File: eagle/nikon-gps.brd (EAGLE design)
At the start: 29.5 x 29.5 mm, 8 parts, among them IC1 GPS-A2235-H, IC2 LP2985SOT, IC3 MAX3370

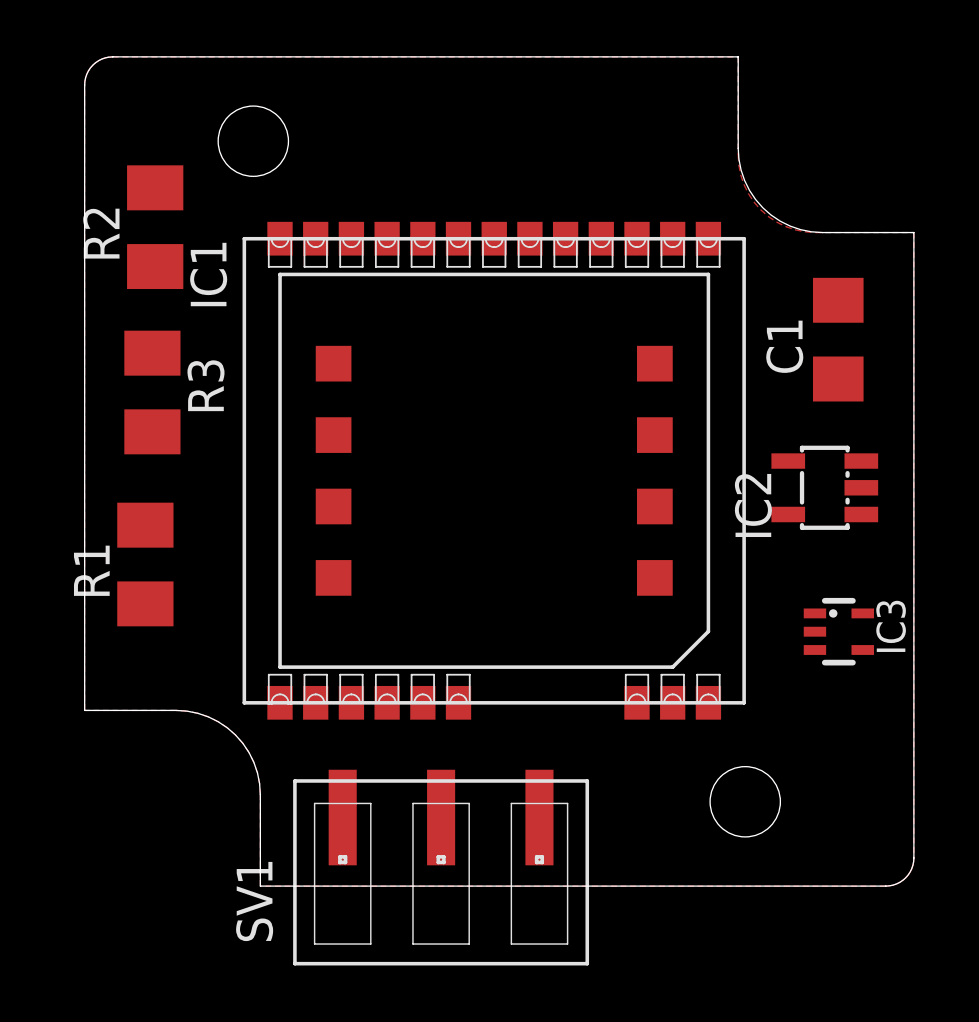
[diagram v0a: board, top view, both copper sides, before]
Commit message: First stab at a PCB layout.
The part placement might still be optimized, esp. if we consider adding
a Status-LED.
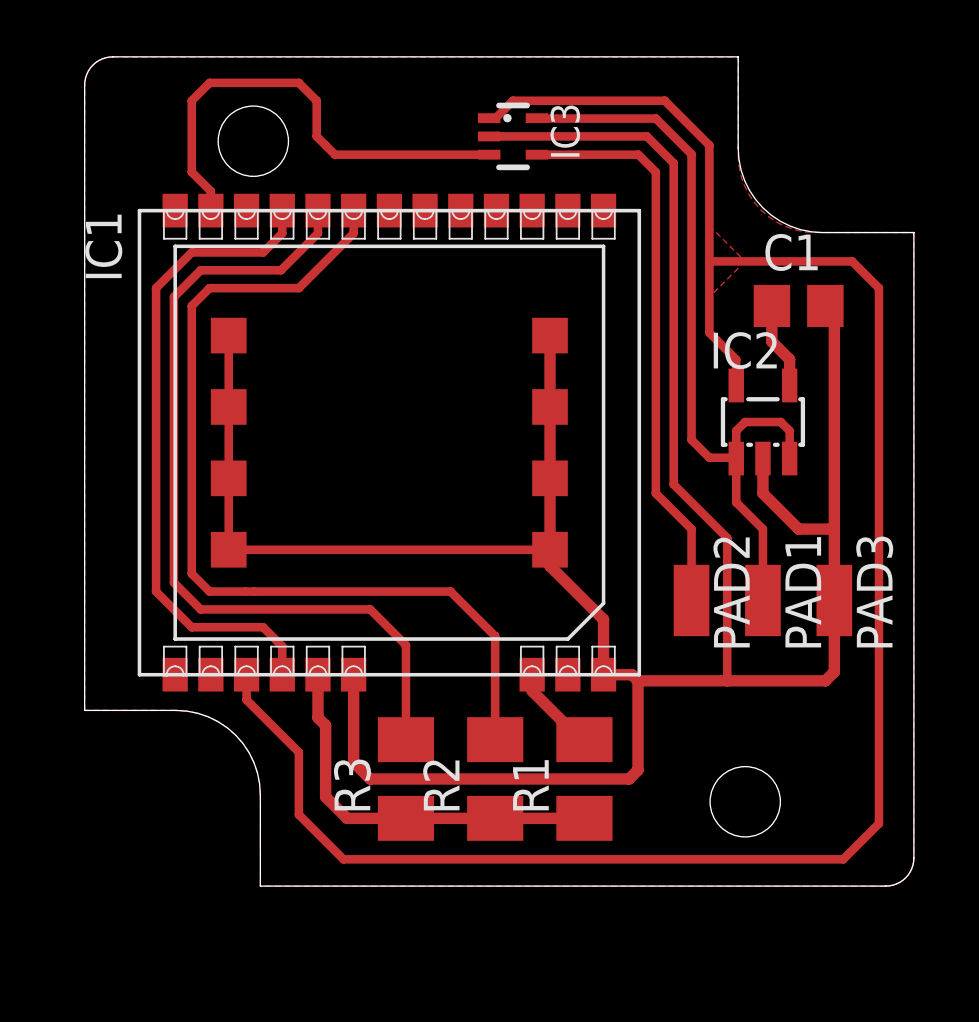
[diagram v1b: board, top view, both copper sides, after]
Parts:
- removed SV1: AKL059-03, selfmade:AKL059-03
- added PAD1, PAD2, PAD3: (no value), wirepad:SMD1,27-2,54
- C1: device rcl:C1206 -> rcl:C0805
- moved R2 23.1 mm to (14.6, 3.81)
- moved IC3 21.1 mm to (15.2, 26.7)
- moved R1 17.4 mm to (17.8, 3.81)
- moved R3 16.4 mm to (11.4, 3.81), turned to 90 degrees
- moved IC1 3.86 mm to (4.49, 11.3)
- moved IC2 3.21 mm to (24.1, 16.5), turned to 0 degrees
- moved C1 1.85 mm to (25.4, 20.6), turned to 0 degrees
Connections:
- net +5V: now also PAD1.1; no longer SV1.1
- net GND: now also PAD3.1; no longer SV1.3
- net N$3: now also PAD2.1; no longer SV1.2
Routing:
- net GND: track 0.00 -> 101.0 mm
- net +3V3: track 0.00 -> 70.7 mm
- net N$6: track 0.00 -> 32.6 mm
- net N$5: track 0.00 -> 29.6 mm
- net +5V: track 0.00 -> 27.6 mm
- net N$7: track 0.00 -> 23.2 mm
- net N$3: track 0.00 -> 20.3 mm
- net N$2: track 0.00 -> 16.8 mm
- net VOUT: track 0.00 -> 14.0 mm
- net N$4: track 0.00 -> 3.16 mm
- net N$1: track 0.00 -> 3.09 mm
- added copper zone on layer 1, net +3V3
- added copper zone on layer 1, net GND
- removed copper zone on layer 1, net GND_NOT_YET

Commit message: Adding missing capacitors for LP2985 voltage regulator.
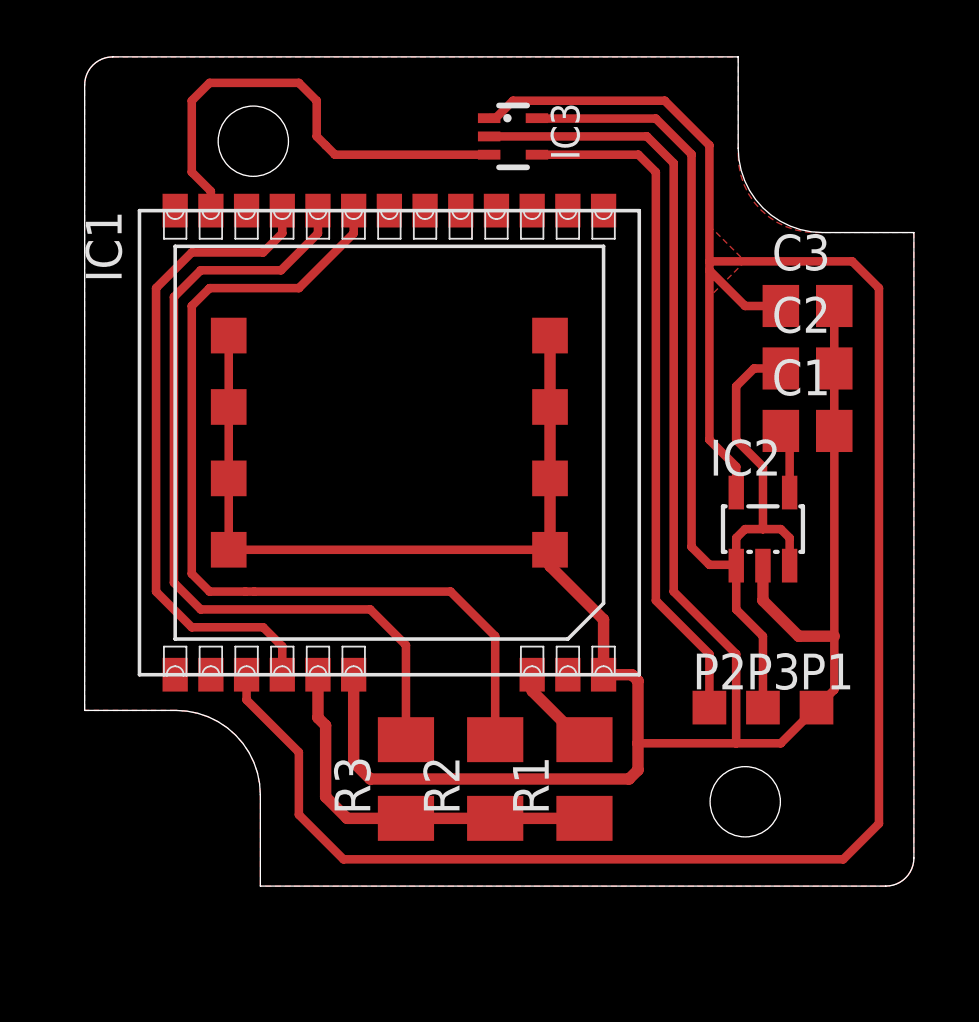
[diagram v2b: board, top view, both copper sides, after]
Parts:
- removed PAD1, PAD2, PAD3: (no value), wirepad:SMD1,27-2,54
- added C2: 1u, rcl:C0805
- added C3: 2u2, rcl:C0805
- added P1, P2, P3: TPTP12SQ, testpad:TP12SQ
- C1: value 100n -> 10n
- moved C1 4.46 mm to (25.7, 16.2)
- moved IC2 3.81 mm to (24.1, 12.7)
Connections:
- net +3V3: now also C3.1
- net +5V: now also C2.1, P3.TP; no longer PAD1.1
- net GND: now also C2.2, C3.2, P1.TP; no longer PAD3.1
- net N$3: now also P2.TP; no longer PAD2.1
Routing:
- net +5V: track 27.6 -> 38.8 mm
- net +3V3: track 70.7 -> 77.6 mm
- net N$3: track 20.3 -> 24.3 mm
- net GND: track 101.0 -> 104.5 mm
- net N$1: track 3.09 -> 2.32 mm

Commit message: Slightly adjusting placement of cable soldering pads.
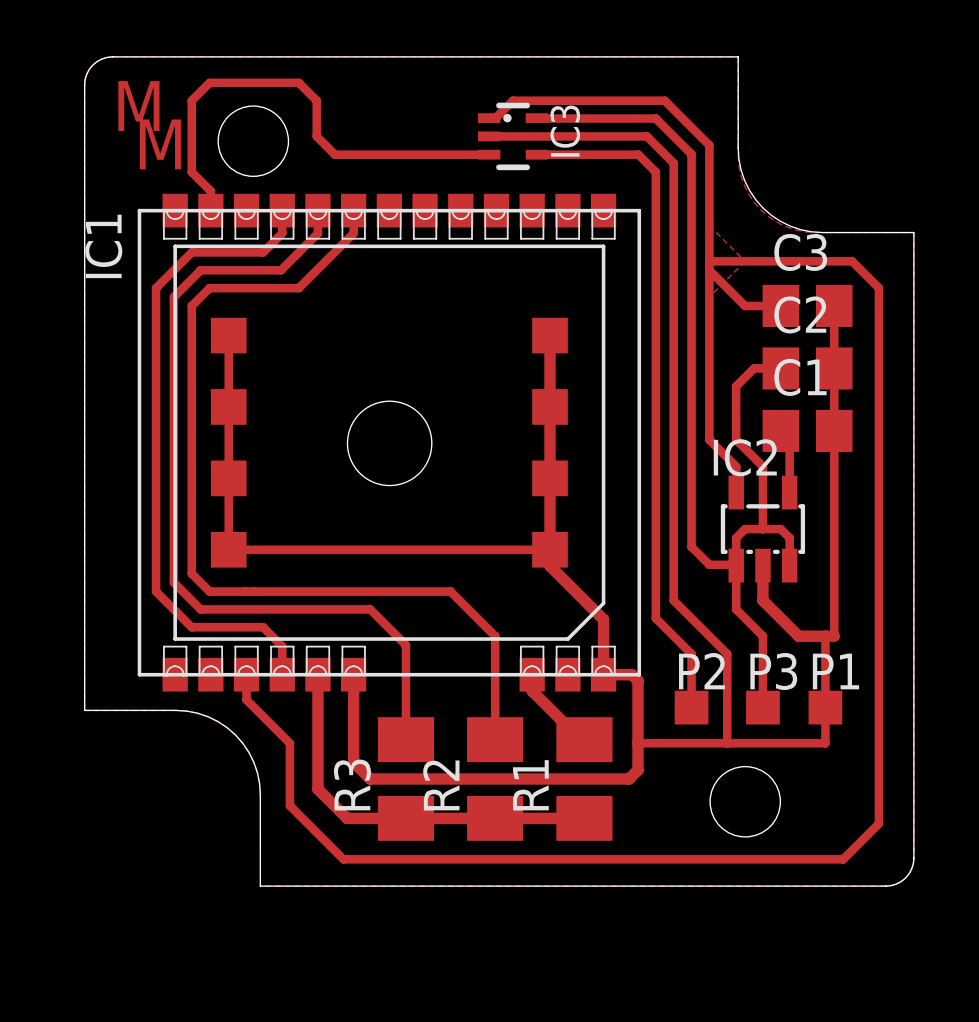
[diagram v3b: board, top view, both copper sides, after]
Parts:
- moved P2 0.64 mm to (21.6, 6.35)
- moved P1 0.32 mm to (26.4, 6.35)
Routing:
- net GND: track 104.5 -> 105.1 mm
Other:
- board text added: "M"
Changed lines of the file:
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@@
 <hole x="23.5" y="3" drill="2.5"/>
 <hole x="6" y="26.5" drill="2.5"/>
+<hole x="10.85" y="15.75" drill="3"/>
+<text x="0.98425" y="26.8605" size="1.778" layer="1" font="vector" ratio="10">M</text>
+<text x="1.74625" y="25.49525" size="1.778" layer="1" font="vector" ratio="10">M</text>
 </plain>
 <attributes>
@@
 <attribute name="TP_SIGNAL_NAME" value="" x="24.13" y="6.35" size="1.778" layer="27" display="off"/>
 </element>
-<element name="P2" library="testpad" package="TP12SQ" value="TPTP12SQ" x="22.225" y="6.35">
-<attribute name="TP_SIGNAL_NAME" value="" x="22.225" y="6.35" size="1.778" layer="27" display="off"/>
+<element name="P2" library="testpad" package="TP12SQ" value="TPTP12SQ" x="21.59" y="6.35">
+<attribute name="TP_SIGNAL_NAME" value="" x="21.59" y="6.35" size="1.778" layer="27" display="off"/>
 </element>
-<element name="P1" library="testpad" package="TP12SQ" value="TPTP12SQ" x="26.035" y="6.35">
-<attribute name="TP_SIGNAL_NAME" value="" x="26.035" y="6.35" size="1.778" layer="27" display="off"/>
+<element name="P1" library="testpad" package="TP12SQ" value="TPTP12SQ" x="26.3525" y="6.35">
+<attribute name="TP_SIGNAL_NAME" value="" x="26.3525" y="6.35" size="1.778" layer="27" display="off"/>
 </element>
 </elements>
@@
 <wire x1="10.16" y1="3.81" x2="19.3675" y2="3.81" width="0.4064" layer="1"/>
 <wire x1="19.3675" y1="3.81" x2="19.685" y2="4.1275" width="0.4064" layer="1"/>
-<wire x1="18.46" y1="7.52" x2="19.4675" y2="7.52" width="0.4064" layer="1"/>
 <wire x1="19.4675" y1="7.52" x2="19.685" y2="7.3025" width="0.4064" layer="1"/>
 <wire x1="19.685" y1="7.3025" x2="19.685" y2="5.08" width="0.4064" layer="1"/>
@@
 <wire x1="14.39" y1="26.67" x2="20.0025" y2="26.67" width="0.3048" layer="1"/>
 <wire x1="20.0025" y1="26.67" x2="20.955" y2="25.7175" width="0.3048" layer="1"/>
-<wire x1="20.955" y1="25.7175" x2="20.955" y2="10.4775" width="0.3048" layer="1"/>
-<wire x1="20.955" y1="10.4775" x2="23.1775" y2="8.255" width="0.3048" layer="1"/>
+<wire x1="20.955" y1="25.7175" x2="20.955" y2="10.16" width="0.3048" layer="1"/>
+<wire x1="20.955" y1="10.16" x2="22.86" y2="8.255" width="0.3048" layer="1"/>
 <wire x1="5.125" y1="19.585" x2="5.125" y2="17.045" width="0.3048" layer="1"/>
 <wire x1="5.125" y1="17.045" x2="5.125" y2="14.505" width="0.3048" layer="1"/>
@@
 <wire x1="24.13" y1="11.4" x2="24.13" y2="10.16" width="0.4064" layer="1"/>
 <wire x1="24.13" y1="10.16" x2="25.4" y2="8.89" width="0.4064" layer="1"/>
-<wire x1="25.4" y1="8.89" x2="26.67" y2="8.89" width="0.4064" layer="1"/>
+<wire x1="25.4" y1="8.89" x2="26.3525" y2="8.89" width="0.4064" layer="1"/>
 <polygon width="0.3048" layer="1" spacing="0.6096" isolate="0.4064">
 <vertex x="0" y="6.25"/>
@@
 <contactref element="C3" pad="2"/>
 <contactref element="P1" pad="TP"/>
-<wire x1="23.1775" y1="5.08" x2="19.685" y2="5.08" width="0.3048" layer="1"/>
-<wire x1="26.035" y1="6.35" x2="26.67" y2="6.985" width="0.3048" layer="1"/>
-<wire x1="26.67" y1="6.985" x2="26.67" y2="8.89" width="0.3048" layer="1"/>
-<wire x1="23.1775" y1="8.255" x2="23.1775" y2="5.08" width="0.3048" layer="1"/>
-<wire x1="23.1775" y1="5.08" x2="24.765" y2="5.08" width="0.3048" layer="1"/>
-<wire x1="24.765" y1="5.08" x2="26.035" y2="6.35" width="0.3048" layer="1"/>
+<wire x1="26.3525" y1="8.89" x2="26.67" y2="8.89" width="0.4064" layer="1"/>
+<wire x1="22.86" y1="5.08" x2="19.685" y2="5.08" width="0.3048" layer="1"/>
+<wire x1="22.86" y1="8.255" x2="22.86" y2="5.08" width="0.3048" layer="1"/>
+<wire x1="22.86" y1="5.08" x2="26.3525" y2="5.08" width="0.3048" layer="1"/>
+<wire x1="26.3525" y1="5.08" x2="26.3525" y2="6.35" width="0.3048" layer="1"/>
 <wire x1="26.6675" y1="20.6375" x2="26.6675" y2="18.415" width="0.3048" layer="1"/>
 <wire x1="26.6675" y1="18.415" x2="26.6675" y2="16.1925" width="0.3048" layer="1"/>
 <wire x1="26.67" y1="8.89" x2="26.67" y2="16.19" width="0.3048" layer="1"/>
 <wire x1="26.67" y1="16.19" x2="26.6675" y2="16.1925" width="0.3048" layer="1"/>
+<wire x1="19.4675" y1="7.52" x2="18.46" y2="7.52" width="0.4064" layer="1"/>
+<wire x1="26.3525" y1="6.35" x2="26.3525" y2="8.89" width="0.3048" layer="1"/>
 </signal>
 <signal name="VANT">
@@
 <wire x1="23.18" y1="14.92" x2="22.225" y2="15.875" width="0.3048" layer="1"/>
 <wire x1="5.76" y1="7.52" x2="5.76" y2="6.6225" width="0.3048" layer="1"/>
-<wire x1="5.76" y1="6.6225" x2="7.62" y2="4.7625" width="0.3048" layer="1"/>
-<wire x1="7.62" y1="4.7625" x2="7.62" y2="2.54" width="0.3048" layer="1"/>
-<wire x1="7.62" y1="2.54" x2="9.2075" y2="0.9525" width="0.3048" layer="1"/>
 <wire x1="9.2075" y1="0.9525" x2="26.9875" y2="0.9525" width="0.3048" layer="1"/>
 <wire x1="26.9875" y1="0.9525" x2="28.2575" y2="2.2225" width="0.3048" layer="1"/>
@@
 <wire x1="24.7675" y1="20.6375" x2="23.495" y2="20.6375" width="0.3048" layer="1"/>
 <wire x1="23.495" y1="20.6375" x2="22.225" y2="21.9075" width="0.3048" layer="1"/>
+<wire x1="9.2075" y1="0.9525" x2="7.3025" y2="2.8575" width="0.3048" layer="1"/>
+<wire x1="7.3025" y1="2.8575" x2="7.3025" y2="5.08" width="0.3048" layer="1"/>
+<wire x1="7.3025" y1="5.08" x2="5.76" y2="6.6225" width="0.3048" layer="1"/>
 </signal>
 <signal name="N$1">
@@
 <wire x1="16.09" y1="26.02" x2="19.7" y2="26.02" width="0.3048" layer="1"/>
 <wire x1="19.7" y1="26.02" x2="20.32" y2="25.4" width="0.3048" layer="1"/>
-<wire x1="20.32" y1="25.4" x2="20.32" y2="10.16" width="0.3048" layer="1"/>
-<wire x1="22.225" y1="8.255" x2="20.32" y2="10.16" width="0.3048" layer="1"/>
+<wire x1="20.32" y1="25.4" x2="20.32" y2="9.525" width="0.3048" layer="1"/>
+<wire x1="21.59" y1="8.255" x2="20.32" y2="9.525" width="0.3048" layer="1"/>
 <contactref element="P2" pad="TP"/>
-<wire x1="22.225" y1="6.35" x2="22.225" y2="8.255" width="0.3048" layer="1"/>
+<wire x1="21.59" y1="6.35" x2="21.59" y2="8.255" width="0.3048" layer="1"/>
 </signal>
 <signal name="N$4">
@@
 <wire x1="14.605" y1="2.41" x2="11.43" y2="2.41" width="0.4064" layer="1"/>
 <wire x1="11.43" y1="2.41" x2="9.3375" y2="2.41" width="0.4064" layer="1"/>
-<wire x1="9.3375" y1="2.41" x2="8.5725" y2="3.175" width="0.4064" layer="1"/>
-<wire x1="8.3" y1="7.52" x2="8.3" y2="5.9875" width="0.4064" layer="1"/>
-<wire x1="8.3" y1="5.9875" x2="8.5725" y2="5.715" width="0.4064" layer="1"/>
-<wire x1="8.5725" y1="5.715" x2="8.5725" y2="3.175" width="0.4064" layer="1"/>
+<wire x1="9.3375" y1="2.41" x2="8.3" y2="3.4475" width="0.4064" layer="1"/>
+<wire x1="8.3" y1="7.52" x2="8.3" y2="3.4475" width="0.4064" layer="1"/>
 </signal>
 <signal name="N$5">
